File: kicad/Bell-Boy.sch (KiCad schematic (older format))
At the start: 13 parts, among them P1 RPi Header, P2 Adafruit NXP Header, P3 LiPo Shim Header, P4 LED Header, P5 Switch Header, P6 MPU6050, P7 MPU6050

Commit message: PCB and other updates
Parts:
- R1, R2: footprint Resistors_ThroughHole:Resistor_Horizontal_RM10mm -> Resistors_ThroughHole:Resistor_Horizontal_RM7mm
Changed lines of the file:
@@
 F 0 "R1" V 4730 3200 50  0000 C CNN
 F 1 "4.7k" V 4650 3200 50  0000 C CNN
-F 2 "Resistors_ThroughHole:Resistor_Horizontal_RM10mm" V 4580 3200 50  0001 C CNN
+F 2 "Resistors_ThroughHole:Resistor_Horizontal_RM7mm" V 4580 3200 50  0001 C CNN
 F 3 "" H 4650 3200 50  0000 C CNN
 	1    4650 3200
@@
 F 0 "R2" V 6130 2900 50  0000 C CNN
 F 1 "270R" V 6050 2900 50  0000 C CNN
-F 2 "Resistors_ThroughHole:Resistor_Horizontal_RM10mm" V 5980 2900 50  0001 C CNN
+F 2 "Resistors_ThroughHole:Resistor_Horizontal_RM7mm" V 5980 2900 50  0001 C CNN
 F 3 "" H 6050 2900 50  0000 C CNN
 	1    6050 2900

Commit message: Automated all calibration.  Updated PCB
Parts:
- removed P2: Adafruit NXP Header, Pin_Headers:Pin_Header_Straight_1x06, symbol CONN_01X06
- added P8: AD0, Pin_Headers:Pin_Header_Straight_1x01, symbol CONN_01X01
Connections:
- wire segments 60 -> 47
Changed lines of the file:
@@
-$EndComp
-$Comp
-L CONN_01X06 P2
-U 1 1 5A734148
-P 6450 2300
-F 0 "P2" H 6450 2650 50  0000 C CNN
-F 1 "Adafruit NXP Header" V 6550 2300 50  0000 C CNN
-F 2 "Pin_Headers:Pin_Header_Straight_1x06" H 6450 2300 50  0001 C CNN
-F 3 "" H 6450 2300 50  0000 C CNN
-	1    6450 2300
-	1    0    0    -1
 $EndComp
 $Comp
@@
 L +3.3V #PWR03
 U 1 1 5A7352E3
-P 5800 2400
-F 0 "#PWR03" H 5800 2250 50  0001 C CNN
-F 1 "+3.3V" H 5800 2540 50  0000 C CNN
-F 2 "" H 5800 2400 50  0000 C CNN
-F 3 "" H 5800 2400 50  0000 C CNN
-	1    5800 2400
+P 7000 2750
+F 0 "#PWR03" H 7000 2600 50  0001 C CNN
+F 1 "+3.3V" H 7000 2890 50  0000 C CNN
+F 2 "" H 7000 2750 50  0000 C CNN
+F 3 "" H 7000 2750 50  0000 C CNN
+	1    7000 2750
 	1    0    0    -1
 $EndComp
@@
 	6200 3000 6350 3000
 Wire Wire Line
-	5800 2400 5800 2550
-Wire Wire Line
-	6000 2350 6600 2350
-Wire Wire Line
-	5800 2550 6250 2550
-Wire Wire Line
-	6250 2150 5550 2150
-Wire Wire Line
-	5550 2150 5550 1900
-Wire Wire Line
-	5550 1900 4550 1900
-Wire Wire Line
-	4550 1900 4550 2150
-Wire Wire Line
-	4550 2150 4800 2150
-Wire Wire Line
-	6250 2250 5600 2250
-Wire Wire Line
-	5600 2250 5600 2750
-Wire Wire Line
-	5600 2750 4550 2750
-Wire Wire Line
-	4550 2750 4550 2250
-Wire Wire Line
-	4550 2250 4800 2250
+	7000 2750 7000 2850
+Wire Wire Line
+	7000 2850 7450 2850
 Wire Wire Line
 	4800 2050 4100 2050
 Wire Wire Line
 	4100 2050 4100 1800
-Wire Wire Line
-	5300 2250 5400 2250
-Wire Wire Line
-	5400 2250 5400 1650
-Wire Wire Line
-	5400 1650 6000 1650
 Wire Wire Line
 	4800 3200 5000 3200
@@
 Wire Wire Line
 	5000 2950 5000 3100
-Wire Wire Line
-	6000 1650 6000 2350
 $Comp
 L CONN_01X04 P6
@@
 Wire Wire Line
 	6850 1450 6850 2100
-Wire Wire Line
-	6350 2300 6350 2250
 $Comp
 L CONN_01X04 P7
@@
 $EndComp
 Wire Wire Line
-	6750 2400 7300 2400
-Wire Wire Line
-	6650 2300 7300 2300
-Wire Wire Line
-	6600 2200 7300 2200
+	6400 2300 7300 2300
 Wire Wire Line
 	6850 2100 7300 2100
-Wire Wire Line
-	6150 2150 6150 1800
-Wire Wire Line
-	6150 1800 6750 1800
-Wire Wire Line
-	6750 1800 6750 2400
 Connection ~ 6850 2400
-Connection ~ 6150 2150
-Wire Wire Line
-	6650 2300 6650 2700
-Wire Wire Line
-	6650 2700 6150 2700
-Wire Wire Line
-	6150 2700 6150 2250
-Connection ~ 6150 2250
 Connection ~ 6850 2300
-Wire Wire Line
-	6600 2350 6600 2200
+$Comp
+L CONN_01X01 P8
+U 1 1 5AABB68B
+P 7650 2850
+F 0 "P8" H 7650 2950 50  0000 C CNN
+F 1 "AD0" V 7750 2850 50  0000 C CNN
+F 2 "Pin_Headers:Pin_Header_Straight_1x01" H 7650 2850 50  0001 C CNN
+F 3 "" H 7650 2850 50  0000 C CNN
+	1    7650 2850
+	1    0    0    -1
+$EndComp
+Wire Wire Line
+	6450 2200 7300 2200
+Wire Wire Line
+	6450 2200 6450 2250
+Wire Wire Line
+	6450 2250 5300 2250
 Connection ~ 6850 2200
-Connection ~ 6250 2350
+Wire Wire Line
+	6400 2300 6400 2750
+Wire Wire Line
+	6400 2750 4550 2750
+Wire Wire Line
+	4550 2750 4550 2250
+Wire Wire Line
+	4550 2250 4800 2250
+Wire Wire Line
+	5800 2400 7300 2400
+Wire Wire Line
+	5800 2400 5800 1800
+Wire Wire Line
+	5800 1800 4550 1800
+Wire Wire Line
+	4550 1800 4550 2150
+Wire Wire Line
+	4550 2150 4800 2150
 $EndSCHEMATC

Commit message: Updates to new case format
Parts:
- removed D1: 1N4148, Diodes_ThroughHole:Diode_DO-35_SOD27_Horizontal_RM10, symbol D
- removed D2, D3, D4: BAT85, Diodes_ThroughHole:Diode_DO-35_SOD27_Horizontal_RM10, symbol D_Schottky
- removed P1: RPi Header, Pin_Headers:Pin_Header_Straight_2x06, symbol CONN_02X06
- removed P3: LiPo Shim Header, Pin_Headers:Pin_Header_Straight_1x03, symbol CONN_01X03
- removed P4: LED Header, Pin_Headers:Pin_Header_Straight_1x02, symbol CONN_01X02
- removed P5: Switch Header, Pin_Headers:Pin_Header_Straight_1x02, symbol CONN_01X02
- removed P6, P7: MPU6050, Pin_Headers:Pin_Header_Straight_1x04, symbol CONN_01X04
- removed P8: AD0, Pin_Headers:Pin_Header_Straight_1x01, symbol CONN_01X01
- removed R1: 4.7k, Resistors_ThroughHole:Resistor_Horizontal_RM7mm, symbol R
- removed R2: 270R, Resistors_ThroughHole:Resistor_Horizontal_RM7mm, symbol R
- added BATT1: Battery_Cell, Connector_PinHeader_2.54mm:PinHeader_1x02_P2.54mm_Vertical, symbol Device:Battery_Cell
- added C1, C10, C11, C12, C2, C3, C9: 100n, Capacitor_SMD:C_1206_3216Metric_Pad1.42x1.75mm_HandSolder, symbol Device:C
- added C13: 2.2uF, Capacitor_SMD:C_1206_3216Metric_Pad1.42x1.75mm_HandSolder, symbol Device:C
- added C14: 2.2uf, Capacitor_SMD:C_1206_3216Metric_Pad1.42x1.75mm_HandSolder, symbol Device:C
- added C4, C5, C6: 4u7, Capacitor_SMD:C_1206_3216Metric_Pad1.42x1.75mm_HandSolder, symbol Device:C
- added C7, C8: 10n, Capacitor_SMD:C_1206_3216Metric_Pad1.42x1.75mm_HandSolder, symbol Device:C
- added D1: BAT54C, Package_TO_SOT_SMD:SOT-23, symbol Diode:BAT54C
- added J1: Conn_01x01_Male, Connector_PinHeader_2.54mm:PinHeader_1x01_P2.54mm_Vertical, symbol Connector:Conn_01x01_Male
- added J2: Conn_01x06, Connector_PinHeader_2.54mm:PinHeader_1x06_P2.54mm_Vertical, symbol Connector_Generic:Conn_01x06
- added J3: Conn_01x04, Connector_PinHeader_2.54mm:PinHeader_1x04_P2.54mm_Vertical, symbol Connector_Generic:Conn_01x04
- added J4: Conn_02x16_Odd_Even, Connector_PinSocket_2.54mm:PinSocket_2x16_P2.54mm_Vertical_SMD, symbol Connector_Generic:Conn_02x16_Odd_Even
- added LED1: LED_Dual_2pin, Connector_PinHeader_2.54mm:PinHeader_1x02_P2.54mm_Vertical, symbol Device:LED_Dual_2pin
- added R1: 82R, Resistor_SMD:R_1206_3216Metric_Pad1.42x1.75mm_HandSolder, symbol Device:R
- added R2, R5, R6: 10K, Resistor_SMD:R_1206_3216Metric_Pad1.42x1.75mm_HandSolder, symbol Device:R
- added R3: 4.7k, Resistor_SMD:R_1206_3216Metric_Pad1.42x1.75mm_HandSolder, symbol Device:R
- added R4, R8: 100k, Resistor_SMD:R_1206_3216Metric_Pad1.42x1.75mm_HandSolder, symbol Device:R
- added R7: 100K, Resistor_SMD:R_1206_3216Metric_Pad1.42x1.75mm_HandSolder, symbol Device:R
- added SW1: SW_DIP_x01, Button_Switch_THT:SW_Tactile_SPST_Angled_PTS645Vx39-2LFS, symbol Switch:SW_DIP_x01
- added U1: ATmega328P-AU, Package_QFP:LQFP-32_7x7mm_P0.8mm, symbol MCU_Microchip_ATmega:ATmega328P-AU
- added U2, U4: MAX40200, Package_TO_SOT_SMD:SOT-23-5, symbol Regulator_Linear:TLV70012_SOT23-5
- added U3: MCP73831-2-OT, Package_TO_SOT_SMD:SOT-23-5, symbol Battery_Management:MCP73831-2-OT
- added U5, U6: ICM-20689, Sensor_Motion:InvenSense_QFN-24_4x4mm_P0.5mm, symbol Sensor_Motion:ICM-20689
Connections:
- net labels added: +3V3, +5V, +BATT, +VSW, VDDA
- wire segments 47 -> 177

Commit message: Update PCB files
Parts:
- C11, C9: value 100n -> 470nF
- R4, R8: value 100k -> 10K
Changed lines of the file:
@@
 P 5900 1800
 F 0 "R4" H 5970 1846 50  0000 L CNN
-F 1 "100k" H 5970 1755 50  0000 L CNN
+F 1 "10K" H 5970 1755 50  0000 L CNN
 F 2 "Resistor_SMD:R_1206_3216Metric_Pad1.42x1.75mm_HandSolder" V 5830 1800 50  0001 C CNN
 F 3 "~" H 5900 1800 50  0001 C CNN
@@
 P 10450 4400
 F 0 "C11" H 10565 4446 50  0000 L CNN
-F 1 "100n" H 10565 4355 50  0000 L CNN
+F 1 "470nF" H 10565 4355 50  0000 L CNN
 F 2 "Capacitor_SMD:C_1206_3216Metric_Pad1.42x1.75mm_HandSolder" H 10488 4250 50  0001 C CNN
 F 3 "~" H 10450 4400 50  0001 C CNN
@@
 P 10400 2550
 F 0 "C9" H 10515 2596 50  0000 L CNN
-F 1 "100n" H 10515 2505 50  0000 L CNN
+F 1 "470nF" H 10515 2505 50  0000 L CNN
 F 2 "Capacitor_SMD:C_1206_3216Metric_Pad1.42x1.75mm_HandSolder" H 10438 2400 50  0001 C CNN
 F 3 "~" H 10400 2550 50  0001 C CNN
@@
 P 6400 1600
 F 0 "R8" V 6193 1600 50  0000 C CNN
-F 1 "100k" V 6284 1600 50  0000 C CNN
+F 1 "10K" V 6284 1600 50  0000 C CNN
 F 2 "Resistor_SMD:R_1206_3216Metric_Pad1.42x1.75mm_HandSolder" V 6330 1600 50  0001 C CNN
 F 3 "~" H 6400 1600 50  0001 C CNN

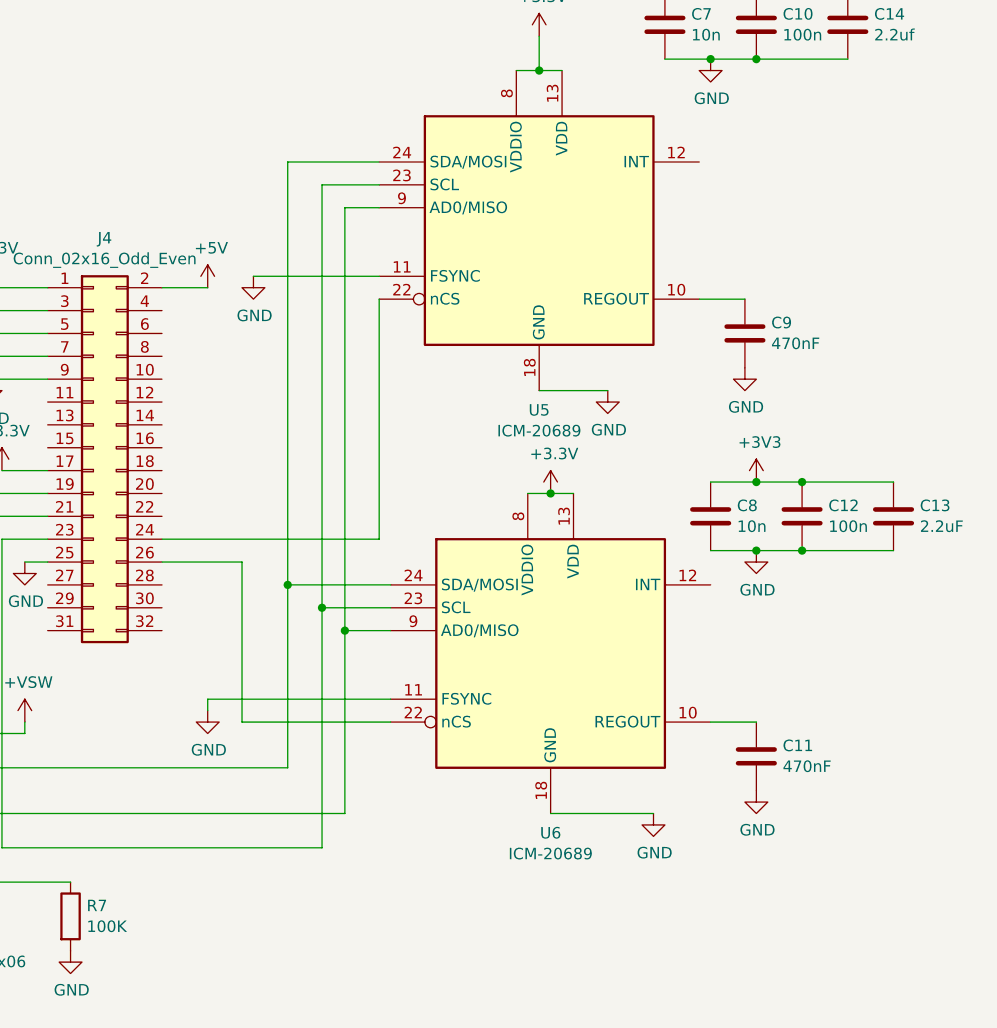
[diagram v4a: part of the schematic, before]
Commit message: Finished autotare and single IMU conversion
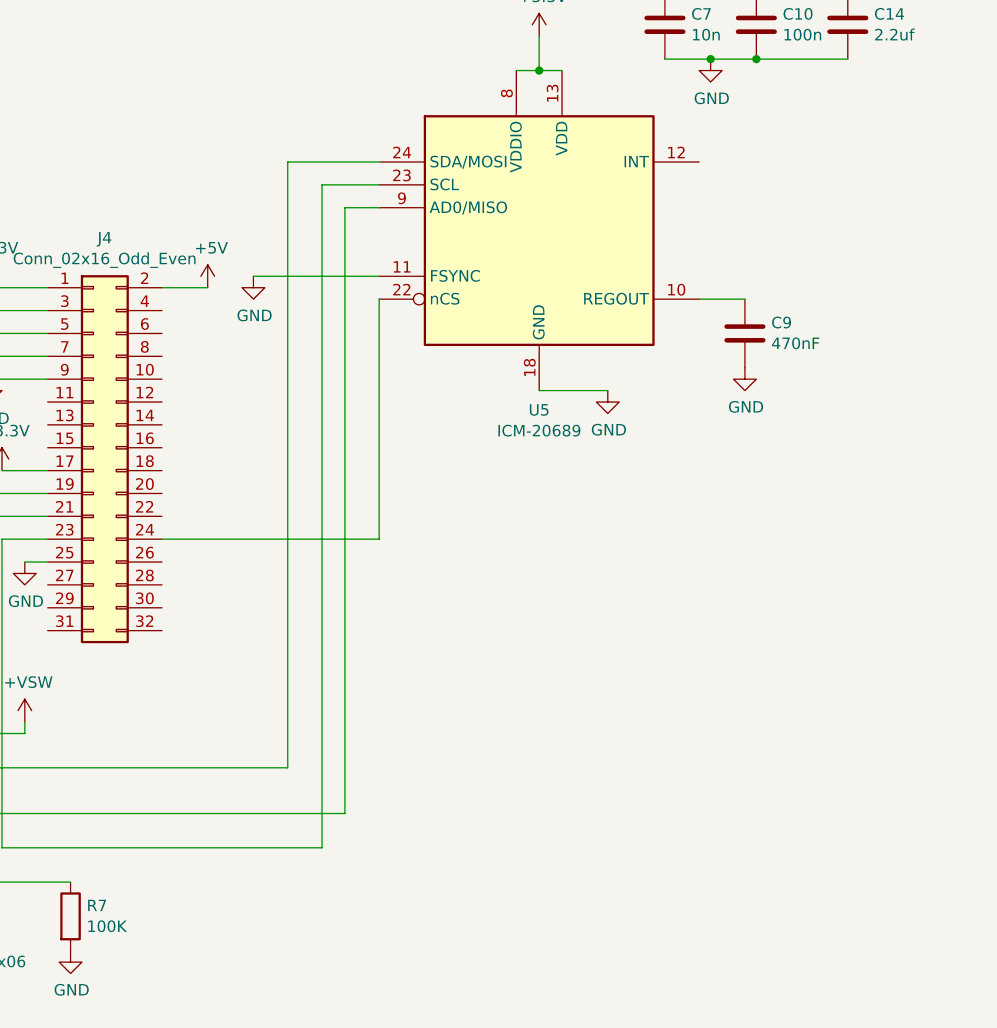
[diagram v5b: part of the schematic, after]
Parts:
- removed C11: 470nF, Capacitor_SMD:C_1206_3216Metric_Pad1.42x1.75mm_HandSolder, symbol Device:C
- removed C12: 100n, Capacitor_SMD:C_1206_3216Metric_Pad1.42x1.75mm_HandSolder, symbol Device:C
- removed C13: 2.2uF, Capacitor_SMD:C_1206_3216Metric_Pad1.42x1.75mm_HandSolder, symbol Device:C
- removed C8: 10n, Capacitor_SMD:C_1206_3216Metric_Pad1.42x1.75mm_HandSolder, symbol Device:C
- removed U6: ICM-20689, Sensor_Motion:InvenSense_QFN-24_4x4mm_P0.5mm, symbol Sensor_Motion:ICM-20689
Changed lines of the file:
@@
 	6950 2550 7350 2550
-Wire Wire Line
-	8850 3650 8400 3650
-Wire Wire Line
-	8400 3650 8400 1800
 Wire Wire Line
 	9400 1400 9500 1400
@@
 Wire Wire Line
 	9500 1400 9600 1400
-Wire Wire Line
-	9450 3250 9550 3250
-$Comp
-L power:+3.3V #PWR0102
-U 1 1 5C5F7340
-P 9550 3250
-F 0 "#PWR0102" H 9550 3100 50  0001 C CNN
-F 1 "+3.3V" H 9565 3423 50  0000 C CNN
-F 2 "" H 9550 3250 50  0001 C CNN
-F 3 "" H 9550 3250 50  0001 C CNN
-	1    9550 3250
-	1    0    0    -1
-$EndComp
-Connection ~ 9550 3250
-Wire Wire Line
-	9550 3250 9650 3250
 $Comp
 L power:GND #PWR0105
@@
 	9500 2800 9800 2800
 $Comp
-L power:GND #PWR0106
-U 1 1 5C611DFA
-P 10000 4650
-F 0 "#PWR0106" H 10000 4400 50  0001 C CNN
-F 1 "GND" H 10005 4477 50  0000 C CNN
-F 2 "" H 10000 4650 50  0001 C CNN
-F 3 "" H 10000 4650 50  0001 C CNN
-	1    10000 4650
-	1    0    0    -1
-$EndComp
-Wire Wire Line
-	9550 4650 10000 4650
-$Comp
 L power:GND #PWR0107
 U 1 1 5C6175DE
@@
 Wire Wire Line
 	8400 1800 8800 1800
-Wire Wire Line
-	8850 3750 8550 3750
-Wire Wire Line
-	8550 3750 8550 1900
-$Comp
-L power:GND #PWR0108
-U 1 1 5C632B81
-P 8050 4200
-F 0 "#PWR0108" H 8050 3950 50  0001 C CNN
-F 1 "GND" H 8055 4027 50  0000 C CNN
-F 2 "" H 8050 4200 50  0001 C CNN
-F 3 "" H 8050 4200 50  0001 C CNN
-	1    8050 4200
-	1    0    0    -1
-$EndComp
-Wire Wire Line
-	8850 4150 8050 4150
-Wire Wire Line
-	8050 4150 8050 4200
 $Comp
 L power:GND #PWR0109
@@
 	10250 1050 10450 1050
 $Comp
-L power:+3V3 #PWR0111
-U 1 1 5C644700
-P 10450 3200
-F 0 "#PWR0111" H 10450 3050 50  0001 C CNN
-F 1 "+3V3" H 10465 3373 50  0000 C CNN
-F 2 "" H 10450 3200 50  0001 C CNN
-F 3 "" H 10450 3200 50  0001 C CNN
-	1    10450 3200
-	1    0    0    -1
-$EndComp
-$Comp
-L power:GND #PWR0112
-U 1 1 5C6447B6
-P 10450 3500
-F 0 "#PWR0112" H 10450 3250 50  0001 C CNN
-F 1 "GND" H 10455 3327 50  0000 C CNN
-F 2 "" H 10450 3500 50  0001 C CNN
-F 3 "" H 10450 3500 50  0001 C CNN
-	1    10450 3500
-	1    0    0    -1
-$EndComp
-$Comp
-L Device:C C8
-U 1 1 5C644810
-P 10250 3350
-F 0 "C8" H 10365 3396 50  0000 L CNN
-F 1 "10n" H 10365 3305 50  0000 L CNN
-F 2 "Capacitor_SMD:C_1206_3216Metric_Pad1.42x1.75mm_HandSolder" H 10288 3200 50  0001 C CNN
-F 3 "~" H 10250 3350 50  0001 C CNN
-	1    10250 3350
-	1    0    0    -1
-$EndComp
-$Comp
-L Device:C C12
-U 1 1 5C644874
-P 10650 3350
-F 0 "C12" H 10765 3396 50  0000 L CNN
-F 1 "100n" H 10765 3305 50  0000 L CNN
-F 2 "Capacitor_SMD:C_1206_3216Metric_Pad1.42x1.75mm_HandSolder" H 10688 3200 50  0001 C CNN
-F 3 "~" H 10650 3350 50  0001 C CNN
-	1    10650 3350
-	1    0    0    -1
-$EndComp
-Wire Wire Line
-	10250 3200 10450 3200
-Connection ~ 10450 3200
-Wire Wire Line
-	10450 3200 10650 3200
-Wire Wire Line
-	10250 3500 10450 3500
-Connection ~ 10450 3500
-Wire Wire Line
-	10450 3500 10650 3500
-$Comp
 L power:+5V #PWR0114
 U 1 1 5C657409
@@
 $EndComp
 $Comp
-L Device:C C11
-U 1 1 5C6648F1
-P 10450 4400
-F 0 "C11" H 10565 4446 50  0000 L CNN
-F 1 "470nF" H 10565 4355 50  0000 L CNN
-F 2 "Capacitor_SMD:C_1206_3216Metric_Pad1.42x1.75mm_HandSolder" H 10488 4250 50  0001 C CNN
-F 3 "~" H 10450 4400 50  0001 C CNN
-	1    10450 4400
-	1    0    0    -1
-$EndComp
-$Comp
-L power:GND #PWR0116
-U 1 1 5C664961
-P 10450 4550
-F 0 "#PWR0116" H 10450 4300 50  0001 C CNN
-F 1 "GND" H 10455 4377 50  0000 C CNN
-F 2 "" H 10450 4550 50  0001 C CNN
-F 3 "" H 10450 4550 50  0001 C CNN
-	1    10450 4550
-	1    0    0    -1
-$EndComp
-Wire Wire Line
-	10250 4250 10450 4250
-$Comp
 L Device:C C9
 U 1 1 5C66B39B
@@
 Wire Wire Line
 	7250 4300 7250 4250
-$Comp
-L Sensor_Motion:ICM-20689 U6
-U 1 1 5C5E5596
-P 9550 3950
-F 0 "U6" H 9550 3164 50  0000 C CNN
-F 1 "ICM-20689" H 9550 3073 50  0000 C CNN
-F 2 "Sensor_Motion:InvenSense_QFN-24_4x4mm_P0.5mm" H 9550 3150 50  0001 C CNN
-F 3 "" H 9550 3800 50  0001 C CNN
-	1    9550 3950
-	1    0    0    -1
-$EndComp
-$Comp
-L Device:C C13
-U 1 1 5C650DC6
-P 11050 3350
-F 0 "C13" H 11165 3396 50  0000 L CNN
-F 1 "2.2uF" H 11165 3305 50  0000 L CNN
-F 2 "Capacitor_SMD:C_1206_3216Metric_Pad1.42x1.75mm_HandSolder" H 11088 3200 50  0001 C CNN
-F 3 "~" H 11050 3350 50  0001 C CNN
-	1    11050 3350
-	1    0    0    -1
-$EndComp
-Wire Wire Line
-	10650 3200 11050 3200
-Connection ~ 10650 3200
-Wire Wire Line
-	10650 3500 11050 3500
-Connection ~ 10650 3500
 Wire Wire Line
 	10450 1050 10850 1050
@@
 	7050 4450 8400 4450
 Wire Wire Line
-	8400 4450 8400 3650
-Connection ~ 8400 3650
-Wire Wire Line
-	8850 3850 8650 3850
-Wire Wire Line
-	8650 3850 8650 2000
-Wire Wire Line
 	8650 2000 8800 2000
 Wire Wire Line
-	8650 3850 8650 4650
-Wire Wire Line
 	8650 4650 7100 4650
 Wire Wire Line
@@
 Wire Wire Line
 	7100 3350 7350 3350
-Connection ~ 8650 3850
 Wire Wire Line
 	7350 3450 7150 3450
@@
 	7150 4800 8550 4800
 Wire Wire Line
-	8550 4800 8550 3750
-Connection ~ 8550 3750
-Wire Wire Line
 	7850 3450 8800 3450
 Wire Wire Line
 	8800 3450 8800 2400
-Wire Wire Line
-	7850 3550 8200 3550
-Wire Wire Line
-	8200 3550 8200 4250
-Wire Wire Line
-	8200 4250 8850 4250
 $Comp
 L Device:R R7
@@
 	6250 1600 5900 1600
 Connection ~ 5900 1600
+Wire Wire Line
+	8400 1800 8400 4450
+Wire Wire Line
+	8550 1900 8550 4800
+Wire Wire Line
+	8650 2000 8650 4650
 $EndSCHEMATC
